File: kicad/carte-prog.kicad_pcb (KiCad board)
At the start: 2 copper layers, 71.1 x 49.8 mm, 14 parts, among them J1 Connecteur côté carte, J2 RJ12, J3 CHOIX ALIM, J4 DB9_Female, U1 LM1117-3.3, U2 MAX232

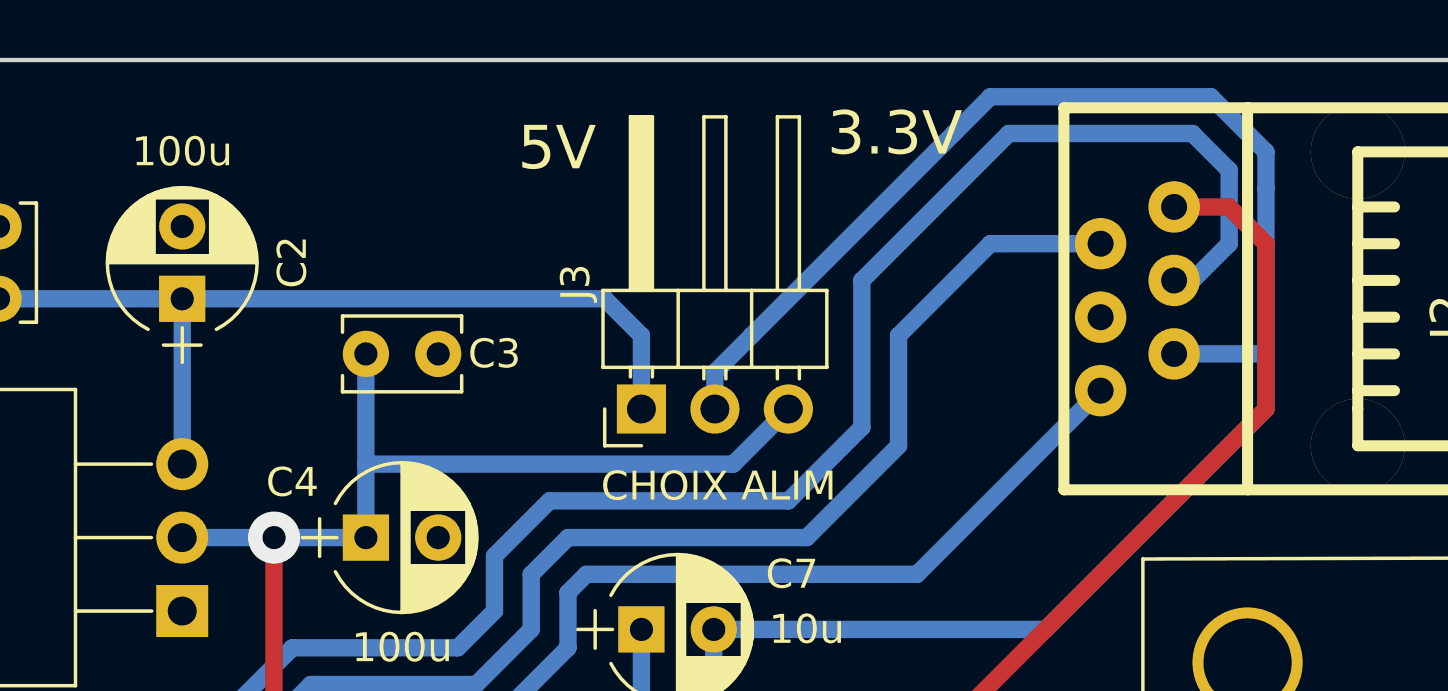
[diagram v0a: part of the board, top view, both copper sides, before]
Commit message: Enlèvement connecteur choix alim
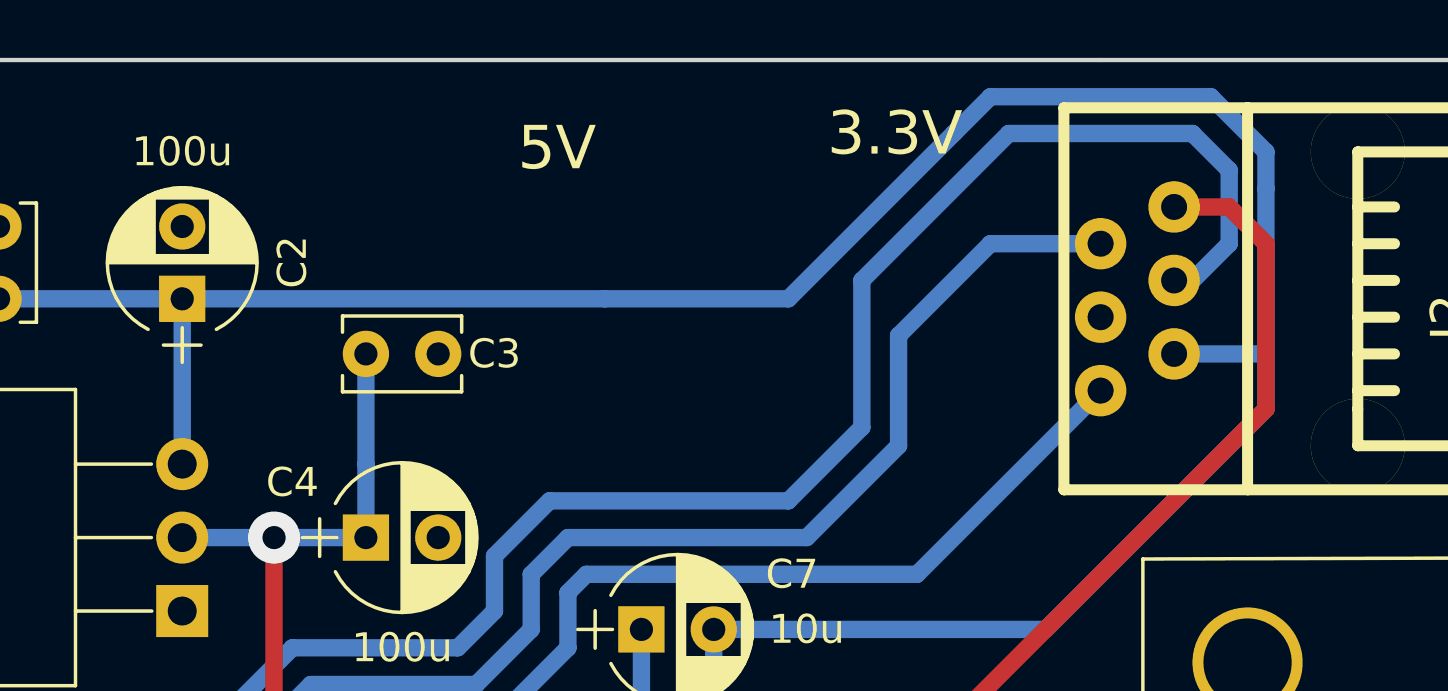
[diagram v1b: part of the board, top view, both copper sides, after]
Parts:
- removed J3: CHOIX ALIM, Pin_Headers:Pin_Header_Angled_1x03_Pitch2.54mm
- J2: value RJ12 -> RJ12 - Côté ordinateur
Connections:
- C7 pad 2: /ALIM -> +5V
- J2 pad 2: /ALIM -> +5V
- U2 pad 16: /ALIM -> +5V
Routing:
- net /ALIM: track 66.9 -> 0.00 mm
- net +5V: track 62.3 -> 126.4 mm
- net +3V3: track 52.5 -> 37.1 mm

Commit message: Préparation des fichiers à la release
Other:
- board text added: "v1.2"
- board text removed: "v1.x"
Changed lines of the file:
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@@
     (links 35)
     (no_connects 0)
-    (area 186.868999 86.284999 258.139001 136.219001)
+    (area 185.455 81.188856 267.175001 136.615001)
     (thickness 1.6)
     (drawings 16)
@@
   (title_block
     (title "Carte programmation")
-    (rev v1.x)
+    (date 2018-04-23)
+    (rev v1.2)
     (company "Ecole Centrale Lyon")
     (comment 1 "Année 2018")
@@
     (effects (font (size 1.5 1.5) (thickness 0.3)))
   )
-  (gr_text v1.x (at 192.024 92.456) (layer F.SilkS)
+  (gr_text v1.2 (at 192.024 92.456) (layer F.SilkS)
     (effects (font (size 1.5 1.5) (thickness 0.3)))
   )
